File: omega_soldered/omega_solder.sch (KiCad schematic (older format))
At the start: 67 parts, among them SW1 SW_Push, U1 ProMicro

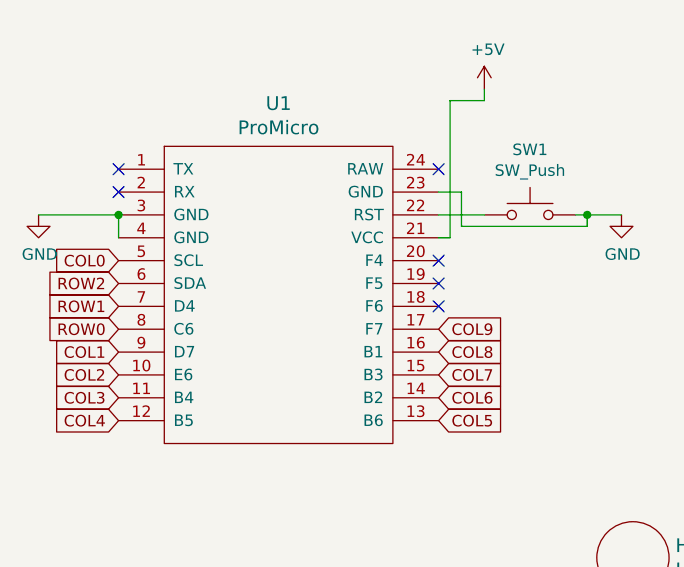
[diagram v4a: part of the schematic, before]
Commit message: do not use series pins on omega soldered
regenerage gerber files for omega soldered and omega 4
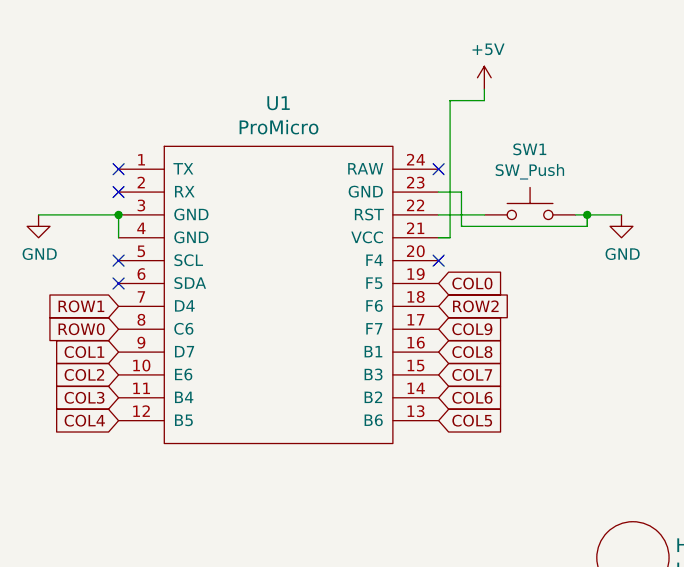
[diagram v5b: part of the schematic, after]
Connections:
- net COL0: now also U1.19 (F5); no longer U1.5 (SCL)
- net ROW2: now also U1.18 (F6); no longer U1.6 (SDA)
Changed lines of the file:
@@
 Text GLabel 2100 2500 0    50   Input ~ 0
 ROW0
-Text GLabel 2100 2200 0    50   Input ~ 0
+Text GLabel 3500 2300 2    50   Input ~ 0
 COL0
-Text GLabel 2100 2300 0    50   Input ~ 0
+Text GLabel 3500 2400 2    50   Input ~ 0
 ROW2
 Text GLabel 2100 2400 0    50   Input ~ 0
@@
 Connection ~ 2100 2000
 NoConn ~ 3500 2200
-NoConn ~ 3500 2300
-NoConn ~ 3500 2400
+NoConn ~ 2100 2200
+NoConn ~ 2100 2300
 $EndSCHEMATC
